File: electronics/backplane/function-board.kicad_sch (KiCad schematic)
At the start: 5 parts, among them X3 MICROMOD_FUNCTION_BOARD_SOCKET

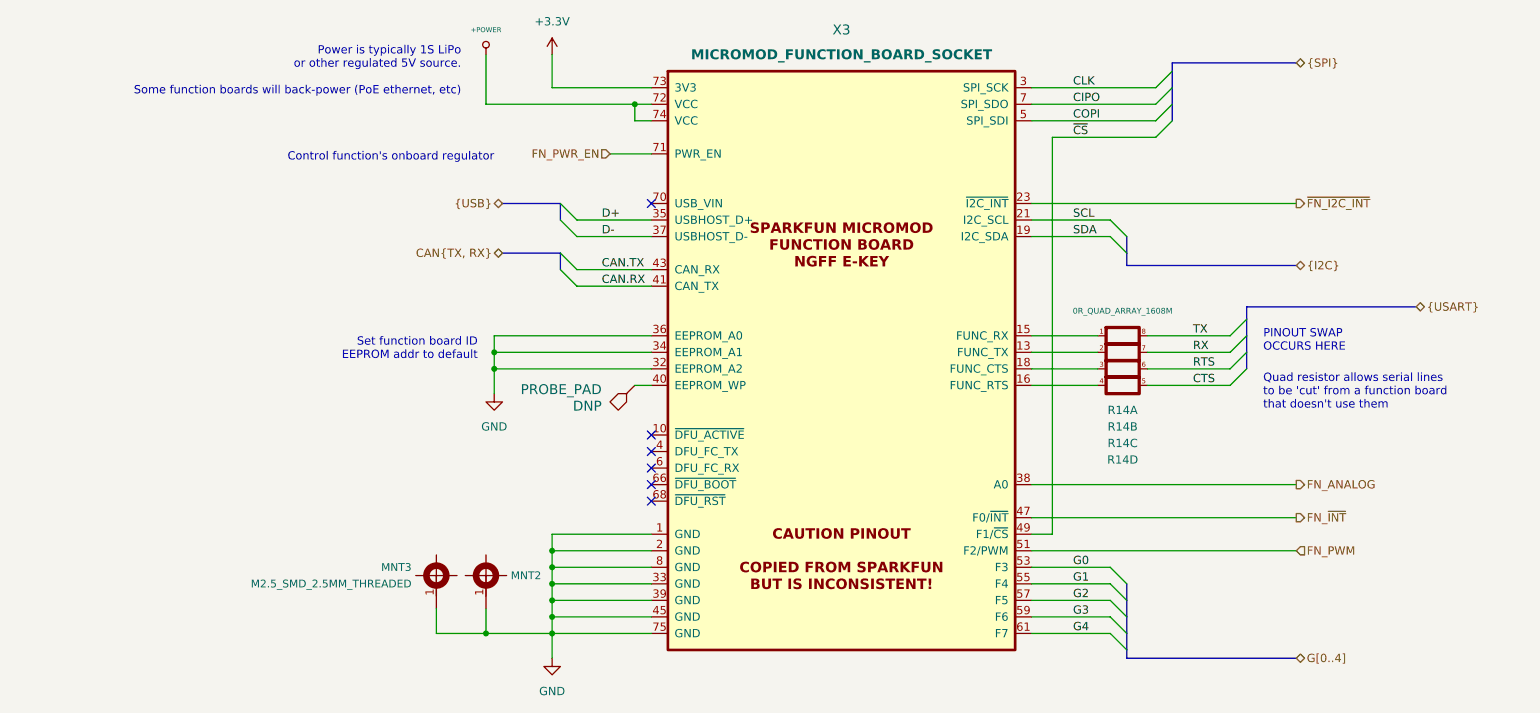
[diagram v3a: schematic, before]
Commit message: Continue backplane design Cleanup schematic, most routing and placement done
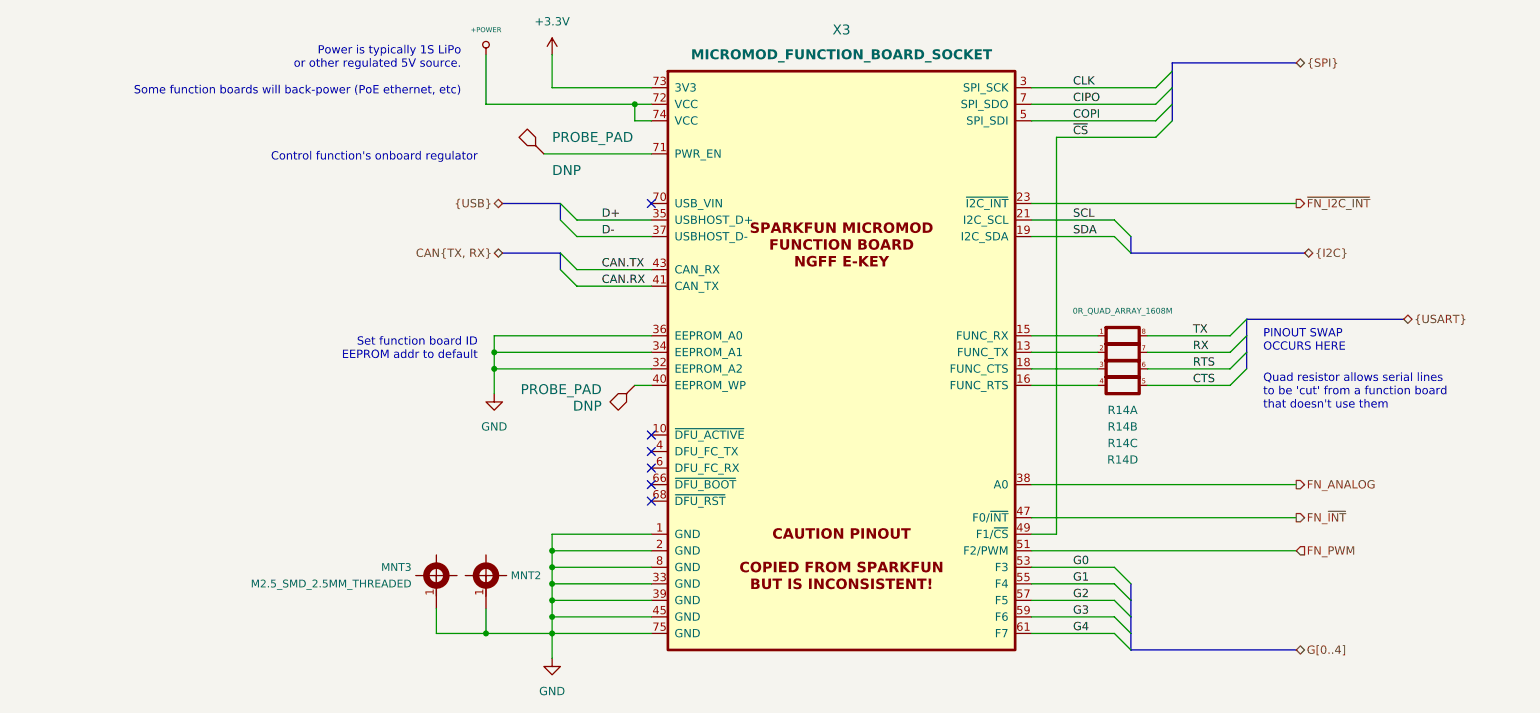
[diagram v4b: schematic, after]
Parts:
- added TEST1: PROBE_PAD, Applidyne_Test:TP200, symbol appli_test_points:PROBE_PAD
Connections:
- net FN_PWR_EN: no longer names the net of X3.71 (PWR_EN)
- net FN_PWR_EN: now also TEST1.1 (PAD)
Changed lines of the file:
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@@
   (no_connect (at 120.65 119.38))
   (no_connect (at 120.65 73.66))
-  (bus_entry (at 191.135 139.7) (size 2.54 2.54)
-    (stroke (width 0) (type default))
-  )
-  (bus_entry (at 191.135 132.08) (size 2.54 2.54)
+  (bus_entry (at 191.77 139.7) (size 2.54 2.54)
+    (stroke (width 0) (type default))
+  )
+  (bus_entry (at 191.77 132.08) (size 2.54 2.54)
     (stroke (width 0) (type default))
   )
@@
     (stroke (width 0) (type default))
   )
-  (bus_entry (at 191.135 137.16) (size 2.54 2.54)
-    (stroke (width 0) (type default))
-  )
-  (bus_entry (at 191.135 76.2) (size 2.54 2.54)
-    (stroke (width 0) (type default))
-  )
-  (bus_entry (at 191.135 129.54) (size 2.54 2.54)
+  (bus_entry (at 191.77 137.16) (size 2.54 2.54)
+    (stroke (width 0) (type default))
+  )
+  (bus_entry (at 191.77 76.2) (size 2.54 2.54)
+    (stroke (width 0) (type default))
+  )
+  (bus_entry (at 191.77 129.54) (size 2.54 2.54)
     (stroke (width 0) (type default))
   )
@@
     (stroke (width 0) (type default))
   )
-  (bus_entry (at 191.135 78.74) (size 2.54 2.54)
+  (bus_entry (at 191.77 78.74) (size 2.54 2.54)
     (stroke (width 0) (type default))
   )
@@
     (stroke (width 0) (type default))
   )
-  (bus_entry (at 191.135 134.62) (size 2.54 2.54)
+  (bus_entry (at 191.77 134.62) (size 2.54 2.54)
     (stroke (width 0) (type default))
   )
@@
     (stroke (width 0) (type default))
   )
-  (bus (pts (xy 212.09 91.44) (xy 212.09 89.535))
-    (stroke (width 0) (type default))
-  )
   (wire (pts (xy 196.85 101.6) (xy 209.55 101.6))
     (stroke (width 0) (type default))
@@
     (stroke (width 0) (type default))
   )
-  (wire (pts (xy 114.3 66.04) (xy 120.65 66.04))
+  (wire (pts (xy 104.14 66.04) (xy 120.65 66.04))
     (stroke (width 0) (type default))
   )
@@
     (stroke (width 0) (type default))
   )
-  (bus (pts (xy 193.675 143.51) (xy 219.71 143.51))
+  (bus (pts (xy 194.31 142.24) (xy 219.71 142.24))
     (stroke (width 0) (type default))
   )
@@
     (stroke (width 0) (type default))
   )
-  (wire (pts (xy 182.245 124.46) (xy 179.07 124.46))
+  (wire (pts (xy 182.88 124.46) (xy 179.07 124.46))
     (stroke (width 0) (type default))
   )
@@
     (stroke (width 0) (type default))
   )
-  (bus (pts (xy 193.675 134.62) (xy 193.675 137.16))
-    (stroke (width 0) (type default))
-  )
   (wire (pts (xy 105.41 127) (xy 120.65 127))
     (stroke (width 0) (type default))
@@
     (stroke (width 0) (type default))
   )
-  (wire (pts (xy 179.07 132.08) (xy 191.135 132.08))
+  (wire (pts (xy 179.07 132.08) (xy 191.77 132.08))
     (stroke (width 0) (type default))
   )
@@
     (stroke (width 0) (type default))
   )
-  (bus (pts (xy 212.09 89.535) (xy 238.125 89.535))
+  (bus (pts (xy 212.09 91.44) (xy 236.22 91.44))
     (stroke (width 0) (type default))
   )
@@
     (stroke (width 0) (type default))
   )
-  (bus (pts (xy 193.675 81.28) (xy 193.675 83.185))
+  (bus (pts (xy 194.31 81.28) (xy 220.98 81.28))
     (stroke (width 0) (type default))
   )
@@
     (stroke (width 0) (type default))
   )
-  (wire (pts (xy 179.07 129.54) (xy 191.135 129.54))
+  (wire (pts (xy 179.07 129.54) (xy 191.77 129.54))
     (stroke (width 0) (type default))
   )
@@
     (stroke (width 0) (type default))
   )
-  (bus (pts (xy 193.675 142.24) (xy 193.675 143.51))
-    (stroke (width 0) (type default))
-  )
   (wire (pts (xy 105.41 124.46) (xy 105.41 127))
     (stroke (width 0) (type default))
@@
     (stroke (width 0) (type default))
   )
-  (wire (pts (xy 179.07 78.74) (xy 191.135 78.74))
-    (stroke (width 0) (type default))
-  )
-  (bus (pts (xy 193.675 139.7) (xy 193.675 142.24))
+  (wire (pts (xy 179.07 78.74) (xy 191.77 78.74))
+    (stroke (width 0) (type default))
+  )
+  (bus (pts (xy 194.31 139.7) (xy 194.31 142.24))
     (stroke (width 0) (type default))
   )
@@
     (stroke (width 0) (type default))
   )
-  (wire (pts (xy 198.12 63.5) (xy 182.245 63.5))
-    (stroke (width 0) (type default))
-  )
-  (bus (pts (xy 193.675 83.185) (xy 219.71 83.185))
+  (wire (pts (xy 198.12 63.5) (xy 182.88 63.5))
     (stroke (width 0) (type default))
   )
@@
     (stroke (width 0) (type default))
   )
-  (wire (pts (xy 182.245 63.5) (xy 182.245 124.46))
+  (wire (pts (xy 182.88 63.5) (xy 182.88 124.46))
     (stroke (width 0) (type default))
   )
@@
     (stroke (width 0) (type default))
   )
-  (bus (pts (xy 193.675 78.74) (xy 193.675 81.28))
+  (bus (pts (xy 194.31 78.74) (xy 194.31 81.28))
     (stroke (width 0) (type default))
   )
@@
     (stroke (width 0) (type default))
   )
-  (bus (pts (xy 193.675 132.08) (xy 193.675 134.62))
+  (bus (pts (xy 194.31 132.08) (xy 194.31 134.62))
     (stroke (width 0) (type default))
   )
@@
     (stroke (width 0) (type default))
   )
-  (wire (pts (xy 179.07 137.16) (xy 191.135 137.16))
+  (wire (pts (xy 179.07 137.16) (xy 191.77 137.16))
     (stroke (width 0) (type default))
   )
@@
     (stroke (width 0) (type default))
   )
-  (wire (pts (xy 179.07 134.62) (xy 191.135 134.62))
+  (wire (pts (xy 179.07 134.62) (xy 191.77 134.62))
     (stroke (width 0) (type default))
   )
@@
     (stroke (width 0) (type default))
   )
-  (wire (pts (xy 179.07 139.7) (xy 191.135 139.7))
+  (wire (pts (xy 179.07 139.7) (xy 191.77 139.7))
     (stroke (width 0) (type default))
   )
@@
     (stroke (width 0) (type default))
   )
+  (bus (pts (xy 194.31 137.16) (xy 194.31 139.7))
+    (stroke (width 0) (type default))
+  )
   (wire (pts (xy 179.07 60.96) (xy 198.12 60.96))
     (stroke (width 0) (type default))
@@
     (stroke (width 0) (type default))
   )
+  (bus (pts (xy 194.31 134.62) (xy 194.31 137.16))
+    (stroke (width 0) (type default))
+  )
   (wire (pts (xy 109.22 83.82) (xy 120.65 83.82))
     (stroke (width 0) (type default))
@@
     (stroke (width 0) (type default))
   )
-  (bus (pts (xy 193.675 137.16) (xy 193.675 139.7))
-    (stroke (width 0) (type default))
-  )
-  (wire (pts (xy 179.07 76.2) (xy 191.135 76.2))
+  (wire (pts (xy 179.07 76.2) (xy 191.77 76.2))
     (stroke (width 0) (type default))
   )
@@
     (effects (font (size 1.27 1.27)) (justify right bottom))
   )
-  (text "Control function's onboard regulator" (at 64.77 67.31 0)
+  (text "Control function's onboard regulator" (at 62.23 67.31 0)
     (effects (font (size 1.27 1.27)) (justify left bottom))
   )
@@
     (effects (font (size 1.27 1.27)) (justify left bottom))
   )
-  (hierarchical_label "{USART}" (shape bidirectional) (at 238.125 89.535 0) (fields_autoplaced)
+  (hierarchical_label "{USART}" (shape bidirectional) (at 236.22 91.44 0) (fields_autoplaced)
     (effects (font (size 1.27 1.27)) (justify left))
   )
@@
     (effects (font (size 1.27 1.27)) (justify left))
   )
-  (hierarchical_label "G[0..4]" (shape bidirectional) (at 219.71 143.51 0) (fields_autoplaced)
-    (effects (font (size 1.27 1.27)) (justify left))
-  )
-  (hierarchical_label "FN_PWR_EN" (shape input) (at 114.3 66.04 180) (fields_autoplaced)
-    (effects (font (size 1.27 1.27)) (justify right))
-  )
-  (hierarchical_label "{I2C}" (shape bidirectional) (at 219.71 83.185 0) (fields_autoplaced)
+  (hierarchical_label "G[0..4]" (shape bidirectional) (at 219.71 142.24 0) (fields_autoplaced)
+    (effects (font (size 1.27 1.27)) (justify left))
+  )
+  (hierarchical_label "{I2C}" (shape bidirectional) (at 220.98 81.28 0) (fields_autoplaced)
     (effects (font (size 1.27 1.27)) (justify left))
   )
@@
         )
       )
+    )
+  )
+  (symbol (lib_id "appli_test_points:PROBE_PAD") (at 104.14 66.04 0) (unit 1)
+    (in_bom yes) (on_board yes) (dnp no)
+    (property "Reference" "TEST1" (at 104.14 68.58 0)
+      (effects (font (size 1.524 1.524)) hide)
+    )
+    (property "Value" "PROBE_PAD" (at 105.41 63.5 0)
+      (effects (font (size 1.524 1.524)) (justify left))
+    )
+    (property "Footprint" "Applidyne_Test:TP200" (at 105.41 64.135 0)
+      (effects (font (size 1.524 1.524)) (justify left) hide)
+    )
+    (property "Datasheet" "" (at 104.14 68.58 0)
+      (effects (font (size 1.524 1.524)))
+    )
+    (property "manf" "N/A" (at 104.14 80.01 0)
+      (effects (font (size 1.524 1.524)) hide)
+    )
+    (property "manf#" "N/A" (at 104.14 82.55 0)
+      (effects (font (size 1.524 1.524)) hide)
+    )
+    (property "Supplier" "N/A" (at 104.14 85.09 0)
+      (effects (font (size 1.524 1.524)) hide)
+    )
+    (property "Supplier URL" "#" (at 104.14 87.63 0)
+      (effects (font (size 1.524 1.524)) hide)
+    )
+    (property "Supplier Price" "0" (at 104.14 77.47 0)
+      (effects (font (size 1.524 1.524)) hide)
+    )
+    (property "Supplier Price Break" "0" (at 104.14 74.93 0)
+      (effects (font (size 1.524 1.524)) hide)
+    )
+    (property "Installed" "DNP" (at 105.41 68.58 0)
+      (effects (font (size 1.524 1.524)) (justify left))
+    )
+    (pin "1")
+    (instances
+      (project "backplane"
+        (path "/0bfdf1e4-b99d-46d4-adfc-42d352d37946/53f921ee-8079-43f9-aa5b-2041db09aea1"
+          (reference "TEST1") (unit 1)
+        )
+      )

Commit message: Backplane routing complete General schematic cleanup, board cosmetics etc
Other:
- title: (none) -> MicroMod Function Board
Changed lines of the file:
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@@
 (kicad_sch (version 20230121) (generator eeschema)
   (paper "A4")
+  (title_block
+    (title "MicroMod Function Board")
+    (date "2023-08-09")
+    (rev "V1.0")
+    (comment 1 "Check function board and processor support before use!")
+    (comment 4 "Accepts Sparkfun's function boards")
+  )
+  (bus_alias "UART" (members "RX" "TX"))
   (bus_alias "USART" (members "TX" "RX" "CTS" "RTS"))
-  (bus_alias "UART" (members "RX" "TX"))
   (junction (at 95.25 139.7) (diameter 0) (color 0 0 0 0)
   )
